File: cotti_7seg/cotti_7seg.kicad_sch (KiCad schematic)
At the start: 1 part, among them J1 Pmod GPIO 2x06 pin

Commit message: feat: cotti 7seg gerbers
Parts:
- removed J1: Pmod GPIO 2x06 pin, Pmod:Pmod_2x06_pin, symbol Pmod:pmod_gpio_2x06_pin
- added J1: Pmod GPIO 2x06 pin, cotti_footprints:Pmod_2x06_pin, symbol cotti_pmod:pmod_gpio_2x06_pin
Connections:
- net GND: now also J1.11 (GND), J1.5 (GND)
- net VCC: now also J1.12 (VCC), J1.6 (VCC)
- net d00: now also J1.1 (IO1)
- net d01: now also J1.2 (IO2/PWM)
- net d02: now also J1.3 (IO3)
- net d03: now also J1.4 (IO4)
- net d10: now also J1.7 (IO5)
- net d11: now also J1.8 (IO6/PWM)
- net d12: now also J1.9 (IO7)
- net d13: now also J1.10 (IO8)
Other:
- company: (none) -> Cotti
- title: (none) -> 7Seg Module
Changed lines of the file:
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@@
 	(generator_version "9.0")
 	(paper "A4")
+	(title_block
+		(title "7Seg Module")
+		(date "2026-01-18")
+		(rev "0.0")
+		(company "Cotti")
+	)
 	(junction
 		(at 120.65 114.3)
@@
 		(dnp no)
 		(fields_autoplaced yes)
-		(property "Reference" "#FLG01"
+		(property "Reference" "#FLG02"
 			(at 122.555 111.76 0)
 			(effects
@@
 			(project ""
 				(path "/1bd78d7c-1eda-4d9f-99db-393243928d6e"
-					(reference "#FLG01")
+					(reference "#FLG02")
 					(unit 1)
 				)
@@
 		(dnp no)
 		(fields_autoplaced yes)
-		(property "Reference" "#FLG02"
+		(property "Reference" "#FLG01"
 			(at 122.555 86.36 0)
 			(effects
@@
 			(project "cotti_7seg"
 				(path "/1bd78d7c-1eda-4d9f-99db-393243928d6e"
-					(reference "#FLG02")
+					(reference "#FLG01")
 					(unit 1)
 				)
@@
 	)
 	(symbol
-		(lib_id "Pmod:pmod_gpio_2x06_pin")
-		(at 114.3 83.82 0)
-		(mirror y)
-		(unit 1)
-		(exclude_from_sim no)
-		(in_bom yes)
-		(on_board yes)
-		(dnp no)
-		(property "Reference" "J1"
-			(at 109.22 82.296 0)
-			(effects
-				(font
-					(size 1.27 1.27)
-				)
-			)
-		)
-		(property "Value" "Pmod GPIO 2x06 pin"
-			(at 109.982 119.126 0)
-			(effects
-				(font
-					(size 1.27 1.27)
-				)
-			)
-		)
-		(property "Footprint" "Pmod:Pmod_2x06_pin"
-			(at 113.284 77.47 0)
-			(effects
-				(font
-					(size 1.27 1.27)
-				)
-				(hide yes)
-			)
-		)
-		(property "Datasheet" "https://app.adam-tech.com/products/download/data_sheet/200508/ph2ra-xx-ua-data-sheet.pdf"
-			(at 110.744 62.992 0)
-			(effects
-				(font
-					(size 1.27 1.27)
-				)
-				(hide yes)
-			)
-		)
-		(property "Description" "Connector Header Through Hole, Right Angle 12 position 0.100\" (2.54mm)"
-			(at 111.76 58.166 0)
-			(effects
-				(font
-					(size 1.27 1.27)
-				)
-				(hide yes)
-			)
-		)
-		(property "Digikey" "https://www.digikey.com/en/products/detail/adam-tech/PH2RA-12-UA/9830569"
-			(at 114.046 55.372 0)
-			(effects
-				(font
-					(size 1.27 1.27)
-				)
-				(hide yes)
-			)
-		)
-		(property "Digikey P/N" "2057-PH2RA-12-UA-ND"
-			(at 113.792 67.818 0)
-			(effects
-				(font
-					(size 1.27 1.27)
-				)
-				(hide yes)
-			)
-		)
-		(property "Mfr." "Adam Tech"
-			(at 113.538 71.374 0)
-			(effects
-				(font
-					(size 1.27 1.27)
-				)
-				(hide yes)
-			)
-		)
-		(property "Mfr. P/N" "PH2RA-12-UA"
-			(at 113.792 74.168 0)
-			(effects
-				(font
-					(size 1.27 1.27)
-				)
-				(hide yes)
-			)
-		)
-		(pin "2"
-		)
-		(pin "3"
-		)
-		(pin "9"
-		)
-		(pin "8"
-		)
-		(pin "10"
-		)
-		(pin "4"
-		)
-		(pin "5"
-		)
-		(pin "6"
-		)
-		(pin "7"
-		)
-		(pin "1"
-		)
-		(pin "12"
-		)
-		(pin "11"
-		)
-		(instances
-			(project ""
-				(path "/1bd78d7c-1eda-4d9f-99db-393243928d6e"
-					(reference "J1")
-					(unit 1)
-				)
-			)
-		)
-	)
-	(symbol
 		(lib_id "power:GND")
 		(at 120.65 115.57 0)
@@
 					(unit 1)
 				)
+			)
+		)
+	)
+	(symbol
+		(lib_id "cotti_pmod:pmod_gpio_2x06_pin")
+		(at 114.3 83.82 0)
+		(mirror y)
+		(unit 1)
+		(exclude_from_sim no)
+		(in_bom yes)
+		(on_board yes)
+		(dnp no)
+		(property "Reference" "J1"
+			(at 108.712 82.296 0)
+			(effects
+				(font
+					(size 1.27 1.27)
+				)
+			)
+		)
+		(property "Value" "Pmod GPIO 2x06 pin"
+			(at 107.442 118.872 0)
+			(effects
+				(font
+					(size 1.27 1.27)
+				)
+			)
+		)
+		(property "Footprint" "cotti_footprints:Pmod_2x06_pin"
+			(at 113.284 77.47 0)
+			(effects
+				(font
+					(size 1.27 1.27)
+				)
+				(hide yes)
+			)
+		)
+		(property "Datasheet" "https://app.adam-tech.com/products/download/data_sheet/200508/ph2ra-xx-ua-data-sheet.pdf"
+			(at 110.744 62.992 0)
+			(effects
+				(font
+					(size 1.27 1.27)
+				)
+				(hide yes)
+			)
+		)
+		(property "Description" "Connector Header Through Hole, Right Angle 12 position 0.100\" (2.54mm)"
+			(at 111.76 58.166 0)
+			(effects
+				(font
+					(size 1.27 1.27)
+				)
+				(hide yes)
+			)
+		)
+		(property "Digikey" "https://www.digikey.com/en/products/detail/adam-tech/PH2RA-12-UA/9830569"
+			(at 114.046 55.372 0)
+			(effects
+				(font
+					(size 1.27 1.27)
+				)
+				(hide yes)
+			)
+		)
+		(property "Mfr." "Adam Tech"
+			(at 113.538 71.374 0)
+			(effects
+				(font
+					(size 1.27 1.27)
+				)
+				(hide yes)
+			)
+		)
+		(property "Mfr. P/N" "PH2RA-12-UA"
+			(at 113.792 74.168 0)
+			(effects
+				(font
+					(size 1.27 1.27)
+				)
+				(hide yes)
+			)
+		)
+		(property "Sim.Device" ""
+			(at 114.3 83.82 0)
+			(effects
+				(font
+					(size 1.27 1.27)
+				)
+				(hide yes)
+			)
+		)
+		(property "Sim.Pins" ""
+			(at 114.3 83.82 0)
+			(effects
+				(font
+					(size 1.27 1.27)
+				)
+				(hide yes)
+			)
+		)
+		(property "Sim.Type" ""
+			(at 114.3 83.82 0)
+			(effects
+				(font
+					(size 1.27 1.27)
+				)
+				(hide yes)
+			)
+		)
+		(pin "5"
+		)
+		(pin "10"
+		)
+		(pin "8"
+		)
+		(pin "3"
+		)
+		(pin "4"
+		)
+		(pin "11"
+		)
+		(pin "12"
+		)
+		(pin "2"
+		)
+		(pin "7"
+		)
+		(pin "6"
+		)
+		(pin "9"
+		)
+		(pin "1"
+		)
+		(instances
+			(project ""
+				(path "/1bd78d7c-1eda-4d9f-99db-393243928d6e"
+					(reference "J1")
+					(unit 1)
+				)

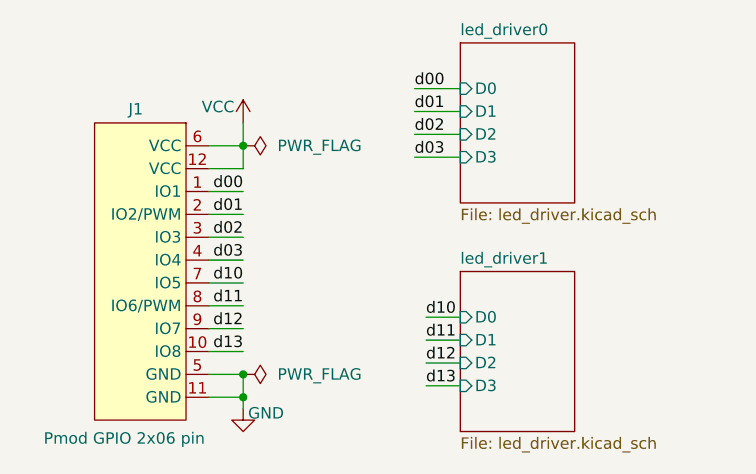
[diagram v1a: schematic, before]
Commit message: fix: change "vcc" to "3v3" power input
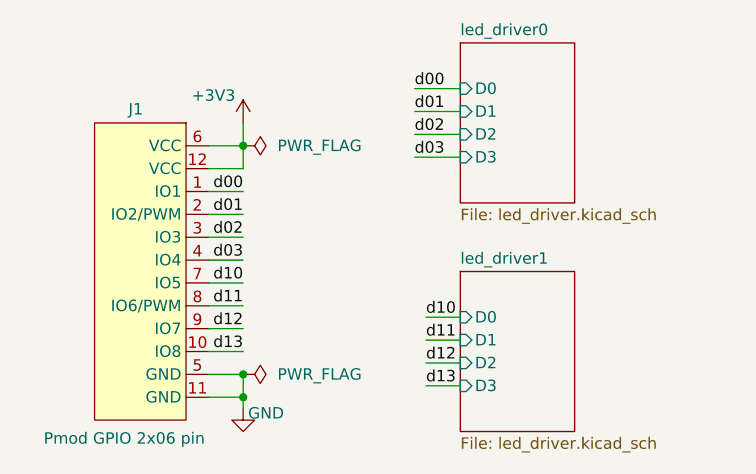
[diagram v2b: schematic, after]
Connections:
- net VCC renamed +3V3
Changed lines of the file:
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@@
+	)
+	(symbol
+		(lib_id "power:+3V3")
+		(at 120.65 83.82 0)
+		(unit 1)
+		(exclude_from_sim no)
+		(in_bom yes)
+		(on_board yes)
+		(dnp no)
+		(property "Reference" "#PWR031"
+			(at 120.65 87.63 0)
+			(effects
+				(font
+					(size 1.27 1.27)
+				)
+				(hide yes)
+			)
+		)
+		(property "Value" "+3V3"
+			(at 117.348 80.772 0)
+			(effects
+				(font
+					(size 1.27 1.27)
+				)
+			)
+		)
+		(property "Footprint" ""
+			(at 120.65 83.82 0)
+			(effects
+				(font
+					(size 1.27 1.27)
+				)
+				(hide yes)
+			)
+		)
+		(property "Datasheet" ""
+			(at 120.65 83.82 0)
+			(effects
+				(font
+					(size 1.27 1.27)
+				)
+				(hide yes)
+			)
+		)
+		(property "Description" "Power symbol creates a global label with name \"+3V3\""
+			(at 120.65 83.82 0)
+			(effects
+				(font
+					(size 1.27 1.27)
+				)
+				(hide yes)
+			)
+		)
+		(pin "1"
+		)
+		(instances
+			(project ""
+				(path "/1bd78d7c-1eda-4d9f-99db-393243928d6e"
+					(reference "#PWR031")
+					(unit 1)
+				)
+			)
+		)
 	)
 	(symbol
@@
 					(unit 1)
 				)
-			)
-		)
-	)
-	(symbol
-		(lib_id "power:VCC")
-		(at 120.65 83.82 0)
-		(unit 1)
-		(exclude_from_sim no)
-		(in_bom yes)
-		(on_board yes)
-		(dnp no)
-		(property "Reference" "#PWR01"
-			(at 120.65 87.63 0)
-			(effects
-				(font
-					(size 1.27 1.27)
-				)
-				(hide yes)
-			)
-		)
-		(property "Value" "VCC"
-			(at 117.856 82.042 0)
-			(effects
-				(font
-					(size 1.27 1.27)
-				)
-			)
-		)
-		(property "Footprint" ""
-			(at 120.65 83.82 0)
-			(effects
-				(font
-					(size 1.27 1.27)
-				)
-				(hide yes)
-			)
-		)
-		(property "Datasheet" ""
-			(at 120.65 83.82 0)
-			(effects
-				(font
-					(size 1.27 1.27)
-				)
-				(hide yes)
-			)
-		)
-		(property "Description" "Power symbol creates a global label with name \"VCC\""
-			(at 120.65 83.82 0)
-			(effects
-				(font
-					(size 1.27 1.27)
-				)
-				(hide yes)
-			)
-		)
-		(pin "1"
-		)
-		(instances
-			(project ""
-				(path "/1bd78d7c-1eda-4d9f-99db-393243928d6e"
-					(reference "#PWR01")
-					(unit 1)
-				)
